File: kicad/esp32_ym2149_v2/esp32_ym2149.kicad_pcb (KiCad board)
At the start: 2 copper layers, 99.9 x 95 mm, 10 parts

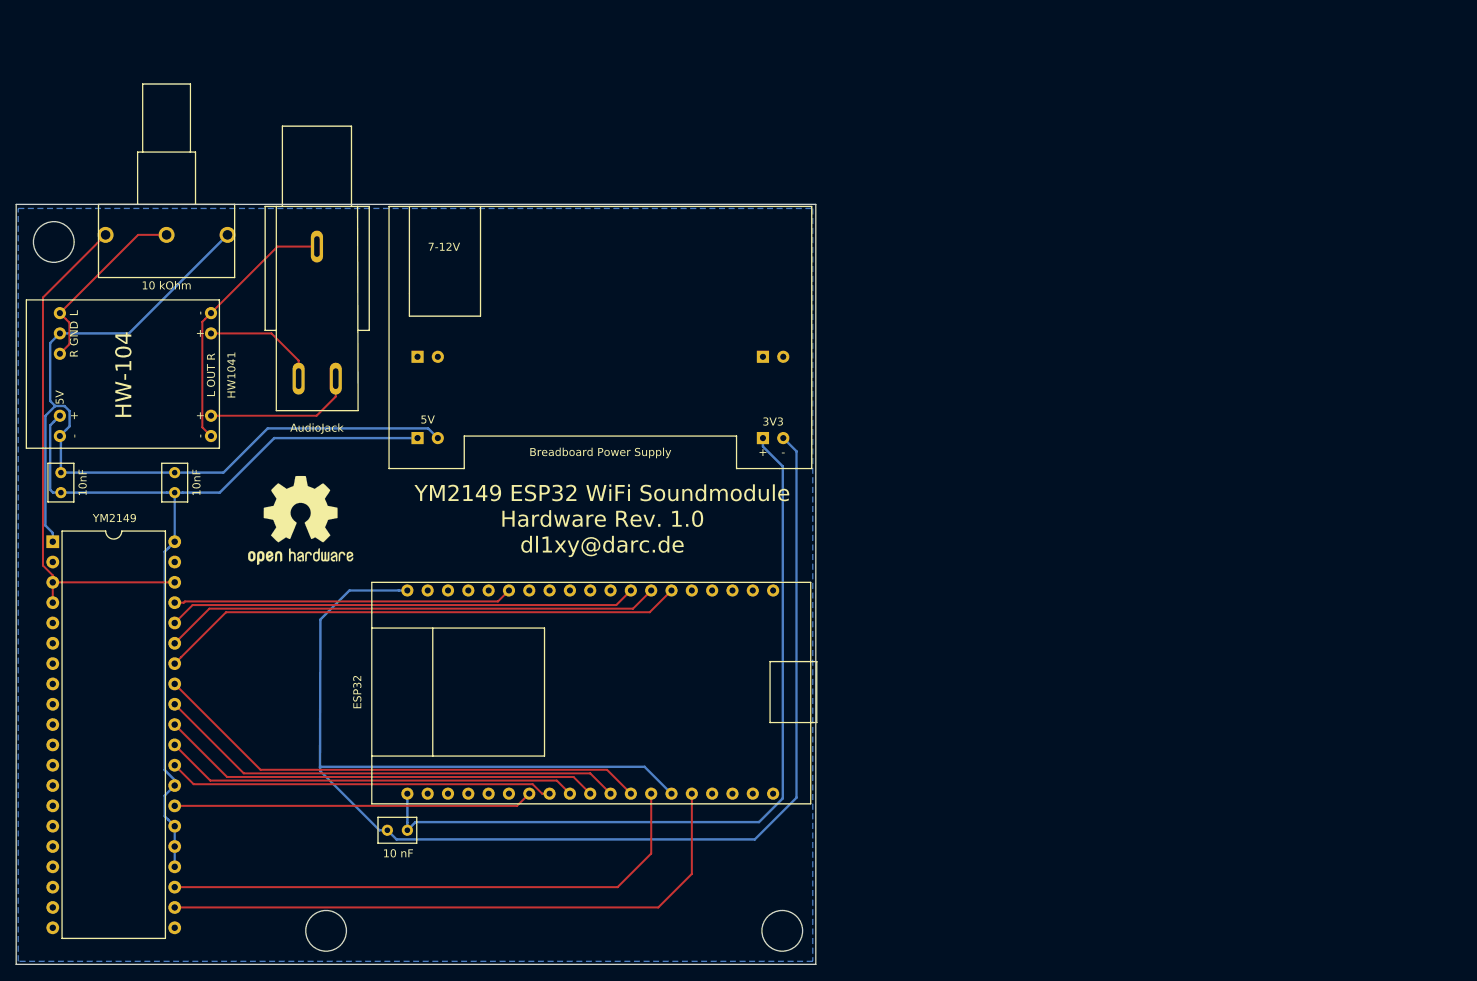
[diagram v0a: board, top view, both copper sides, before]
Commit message: pcb modified, wifi jumper added
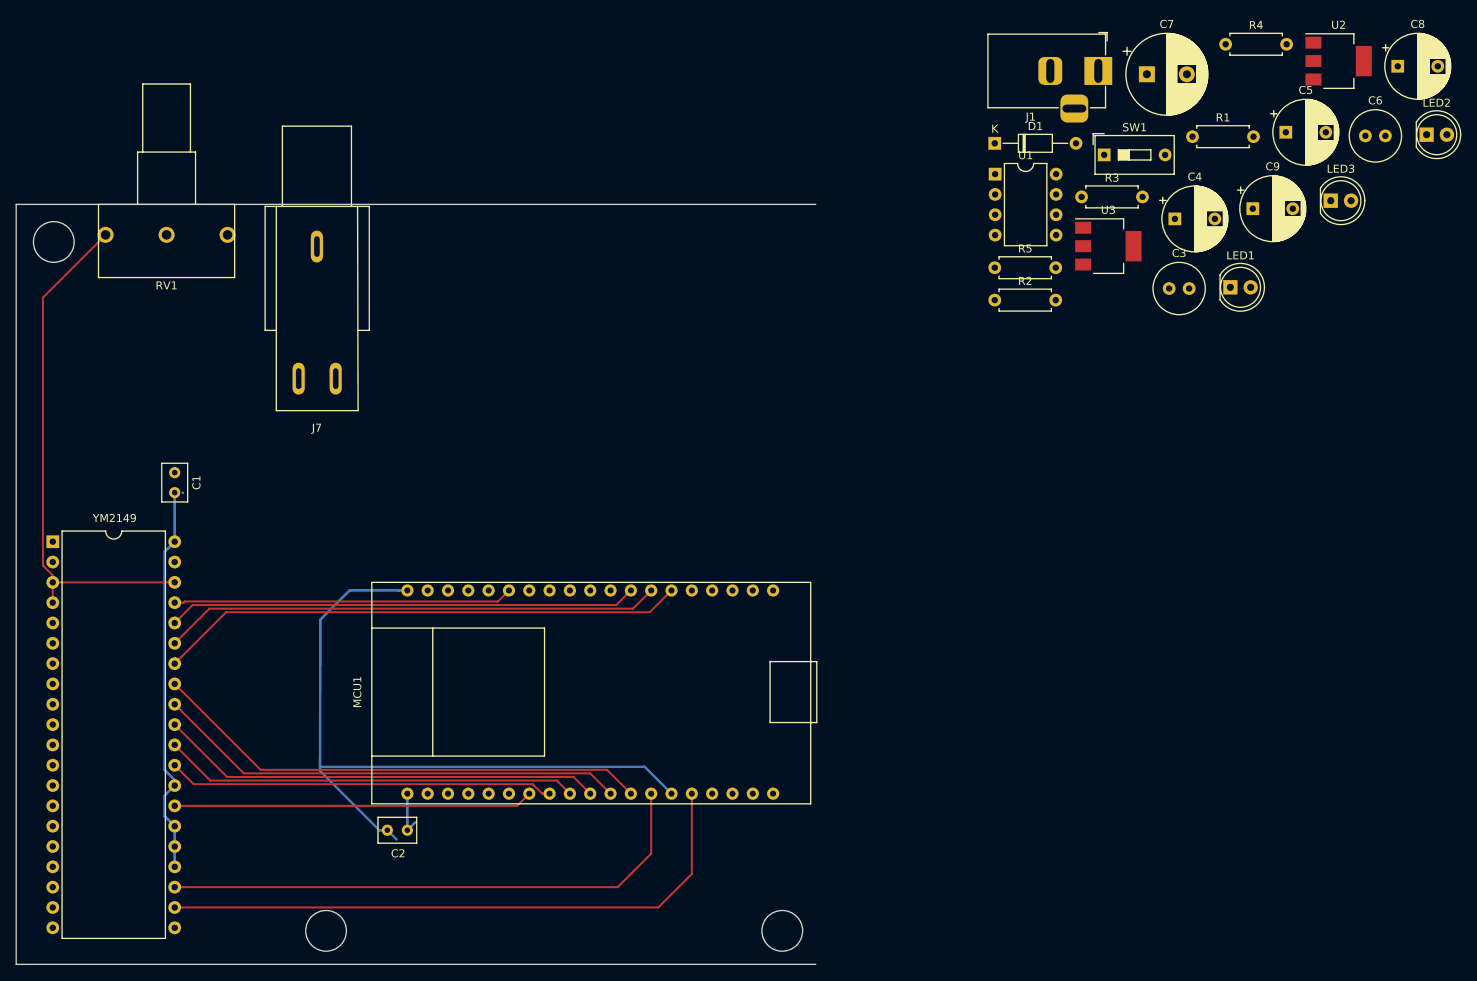
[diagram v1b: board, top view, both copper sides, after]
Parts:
- removed 10nF: 10nF, Capacitor_THT:C_Rect_L4.6mm_W3.0mm_P2.50mm_MKS02_FKP02
- removed Breadboard Power Supply: BreadboardPowerSupply, dl1xy:Breadboard_Powersupply_3V3_5V
- removed HW1041: HW-104_Board, dl1xy:HW-104 Board
- removed REF**: OSHW-Logo2_14.6x12mm_SilkScreen, Symbol:OSHW-Logo2_14.6x12mm_SilkScreen
- added C3: 0.1uF, Capacitor_THT:C_Radial_D6.3mm_H5.0mm_P2.50mm, F.Cu at (257.9, 48.6)
- added C4: 10uF, Capacitor_THT:CP_Radial_D8.0mm_P5.00mm, F.Cu at (258.6, 39.9)
- added C5: 10uF, Capacitor_THT:CP_Radial_D8.0mm_P5.00mm, F.Cu at (272.5, 29.1)
- added C6: 0.1uF, Capacitor_THT:C_Radial_D6.3mm_H5.0mm_P2.50mm, F.Cu at (282.4, 29.5)
- added C7: 100uF, Capacitor_THT:CP_Radial_D10.0mm_P5.00mm, F.Cu at (255.1, 21.8)
- added C8: 22uF, Capacitor_THT:CP_Radial_D8.0mm_P5.00mm, F.Cu at (286.5, 20.8)
- added C9: 22uF, Capacitor_THT:CP_Radial_D8.0mm_P5.00mm, F.Cu at (268.4, 38.6)
- added D1: 1N5400, Diode_THT:D_DO-35_SOD27_P10.16mm_Horizontal, F.Cu at (236.1, 30.5)
- added J1: 9V DC, Connector_BarrelJack:BarrelJack_Horizontal, F.Cu at (249.1, 21.4)
- added LED1: POWER_LED, LED_THT:LED_D5.0mm, F.Cu at (265.6, 48.5)
- added LED2: 3V3_LED, LED_THT:LED_D5.0mm, F.Cu at (290.1, 29.4)
- added LED3: 5V_LED, LED_THT:LED_D5.0mm, F.Cu at (278.1, 37.6)
- added R1: 1.2K, Resistor_THT:R_Axial_DIN0207_L6.3mm_D2.5mm_P7.62mm_Horizontal, F.Cu at (260.8, 29.6)
- added R2: 1.2K, Resistor_THT:R_Axial_DIN0207_L6.3mm_D2.5mm_P7.62mm_Horizontal, F.Cu at (236.1, 50.1)
- added R3: 1k, Resistor_THT:R_Axial_DIN0207_L6.3mm_D2.5mm_P7.62mm_Horizontal, F.Cu at (247.0, 37.2)
- added R4: 520, Resistor_THT:R_Axial_DIN0207_L6.3mm_D2.5mm_P7.62mm_Horizontal, F.Cu at (265.0, 18.1)
- added R5: 220, Resistor_THT:R_Axial_DIN0207_L6.3mm_D2.5mm_P7.62mm_Horizontal, F.Cu at (236.1, 46.0)
- added SW1: SW_SPST, Button_Switch_THT:SW_DIP_SPSTx01_Slide_9.78x4.72mm_W7.62mm_P2.54mm, F.Cu at (249.8, 31.9)
- added U1: LM386, Package_DIP:DIP-8_W7.62mm, F.Cu at (236.2, 34.3)
- added U2: AMS1117-5.0, Package_TO_SOT_SMD:SOT-223-3_TabPin2, F.Cu at (279.1, 20.2)
- added U3: AMS1117-3.3, Package_TO_SOT_SMD:SOT-223-3_TabPin2, F.Cu at (250.3, 43.3)
- C2: renamed from 10 nF
- RV1: renamed from 10 kOhm
- renumbered 10nF to C1, AudioJack to J7, ESP32 to MCU1
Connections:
- net Net-(RV1-Pad3) renamed /RAWAUDIO
- J7 pad R: Net-(HW1041-Pad8) -> Net-(J7-PadR)
- J7 pad S: Net-(HW1041-Pad6) -> GNDREF
- J7 pad T: Net-(HW1041-Pad7) -> Net-(J7-PadR)
- RV1 pad 2: Net-(HW1041-Pad1) -> RV_AUDIO
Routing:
- net GNDREF: track 301.5 -> 89.7 mm
- net +3.3V: track 99.5 -> 6.25 mm
- net +5V: track 107.6 -> 48.9 mm
- net Net-(HW1041-Pad6): track 33.0 -> 0.00 mm
- net Net-(HW1041-Pad1): track 23.4 -> 0.00 mm
- net Net-(HW1041-Pad8): track 18.8 -> 0.00 mm
- net Net-(HW1041-Pad7): track 14.6 -> 0.00 mm
- removed copper zone on B.Cu, net GNDREF
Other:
- board text removed: "YM2149 ESP32 WiFi Soundmodule Hardware Rev. 1.0 dl1xy@darc.de"
